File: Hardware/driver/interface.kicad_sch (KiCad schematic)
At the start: 34 parts

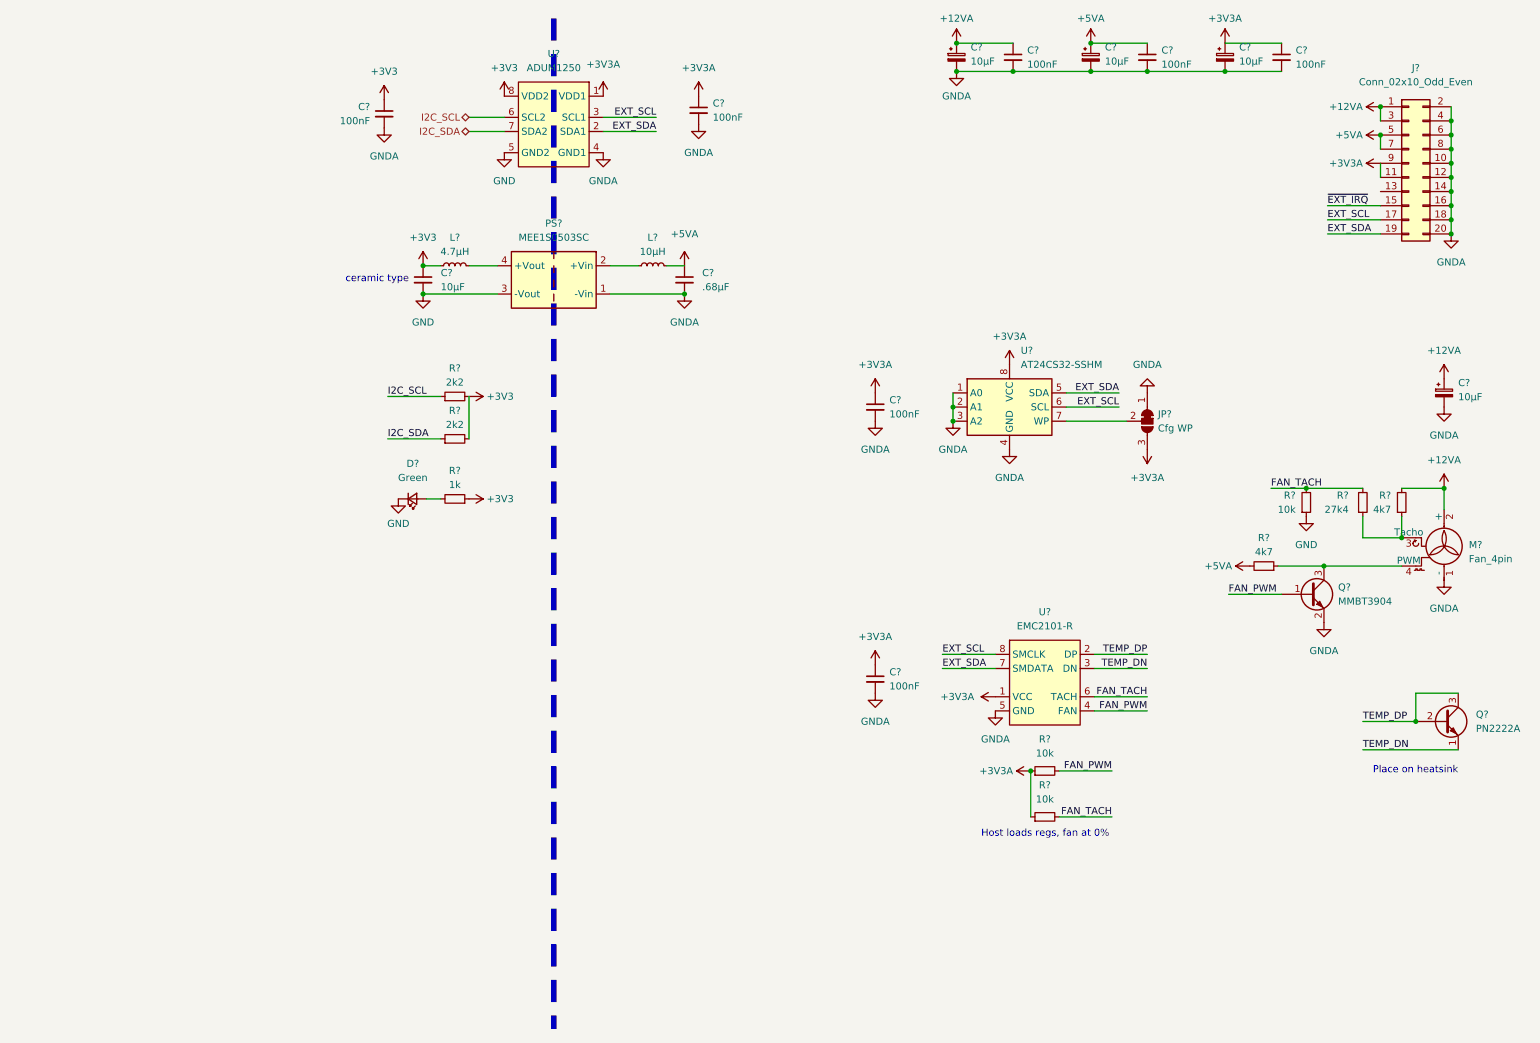
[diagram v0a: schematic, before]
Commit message: Placed all peripherals, start input
- Created footprints/symbols for some required I2C devices, including
  all DACs and ADCs, and placed them on the input section schematic

- Started work on heatsink footprint (C40-058-AE)

- Placed input connector for input. This is a pluggable screw terminal,
  which would then in turn connect to front panel jacks/banana plugs for
  external connectivity. This is good for roughly 20A, which is what the
  fuse (and our maximum rating for now) shall be
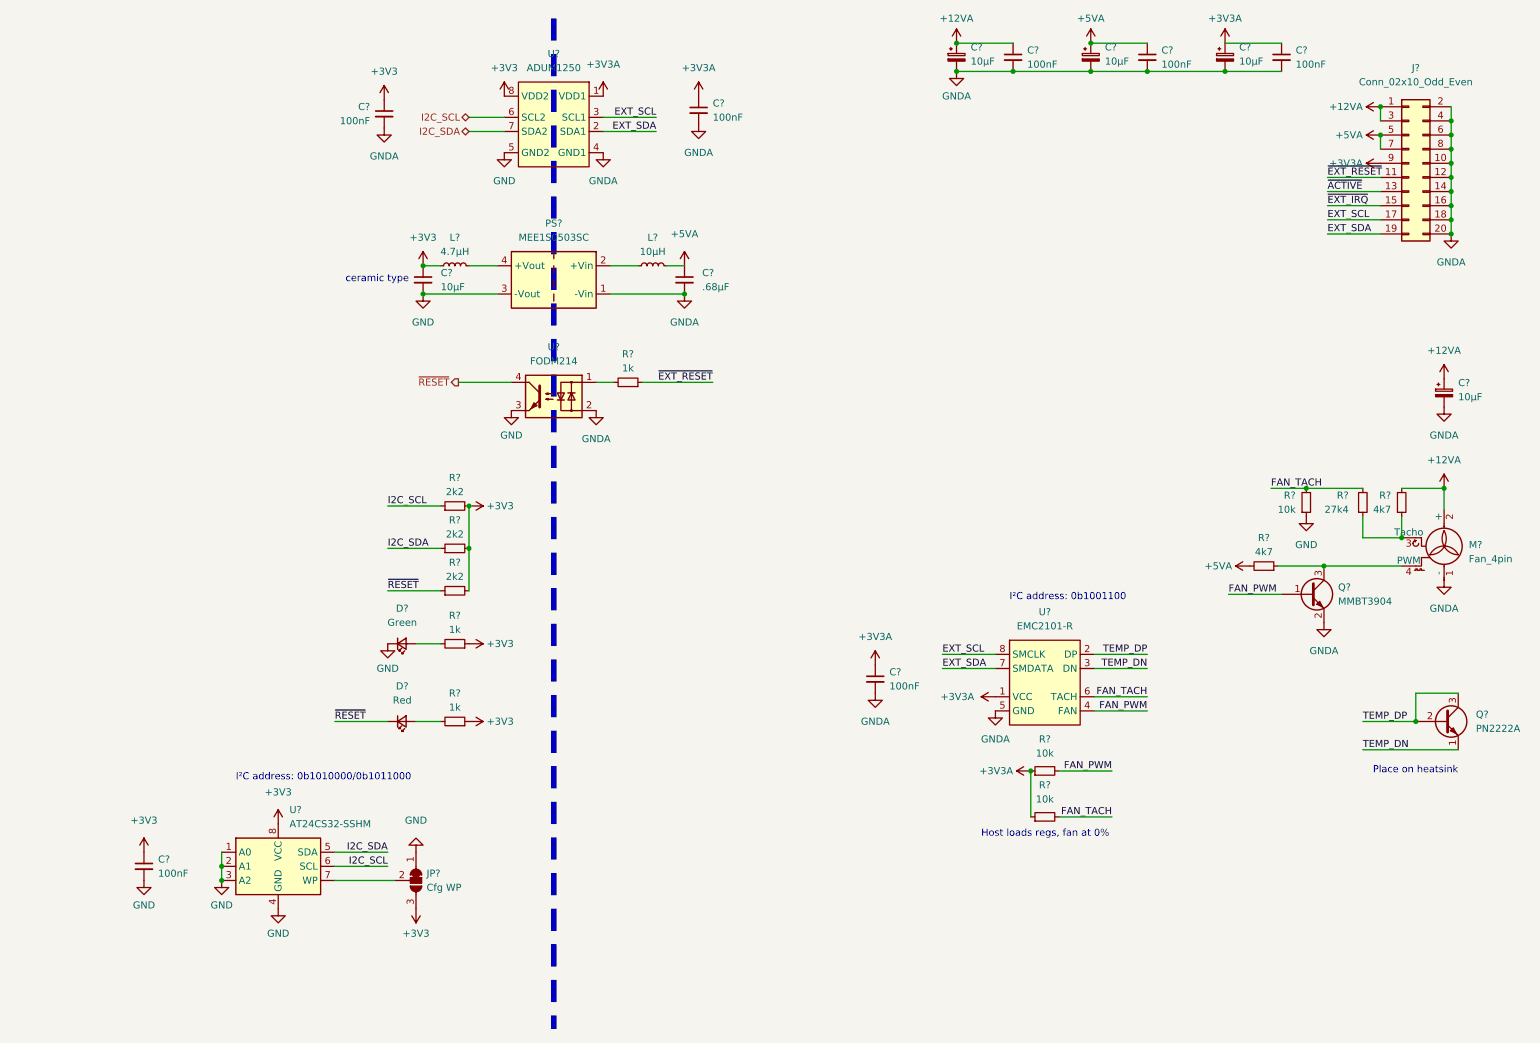
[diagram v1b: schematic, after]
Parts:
- added D?: Red, symbol Device:LED_Small
- added R?: 2k2, Resistor_SMD:R_0805_2012Metric_Pad1.20x1.40mm_HandSolder, symbol Device:R_Small
- added R? (x2): 1k, Resistor_SMD:R_0805_2012Metric_Pad1.20x1.40mm_HandSolder, symbol Device:R_Small
- added U?: FODM214, Package_SO:SOP-4_4.4x2.6mm_P1.27mm, symbol Isolator:FODM214
- C? (x7): footprint (none) -> Capacitor_SMD:C_0805_2012Metric_Pad1.18x1.45mm_HandSolder
- C?: footprint (none) -> Capacitor_SMD:C_0805_2012Metric_Pad1.18x1.45mm_HandSolder; MPN (none) -> CL21A106KPFNNNF
- C?: footprint (none) -> Capacitor_SMD:C_0805_2012Metric_Pad1.18x1.45mm_HandSolder; MPN (none) -> CL21B684JOFNNNE
- D?: MPN (none) -> 150080VS75000
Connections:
- net +3V3: now also C?.1, JP?.3 (B), U?.8 (VCC), R?.1, R?.2
- net +3V3A: no longer C?.1, J?.11 (Pin_11), JP?.3 (B), U?.8 (VCC)
- net EXT_SCL: no longer U?.6 (SCL)
- net EXT_SDA: no longer U?.5 (SDA)
- net GND: now also C?.2, JP?.1 (A), U?.1 (A0), U?.2 (A1), U?.3 (A2), U?.4 (GND), U?.3
- net GNDA: now also U?.2; no longer C?.2, JP?.1 (A), U?.1 (A0), U?.2 (A1), U?.3 (A2), U?.4 (GND)
- net I2C_SCL: now also U?.6 (SCL)
- net I2C_SDA: now also U?.5 (SDA)
- net ~{ACTIVE}: now reaches J?.13 (Pin_13)
- new net: R?.2, U?.1
- new net: D?.2 (A), R?.2
- new net ~{EXT_RESET}: J?.11 (Pin_11), R?.1
- new net ~{RESET}: D?.1 (K), R?.1, U?.4
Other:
- note added: "I²C address: 0b1001100"
- note added: "I²C address: 0b1010000/0b1011000"
- moved on the sheet: C?, D?, JP?, R?, U?

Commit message: Basic board layout shape
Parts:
- gave numbers to parts that had none: 39

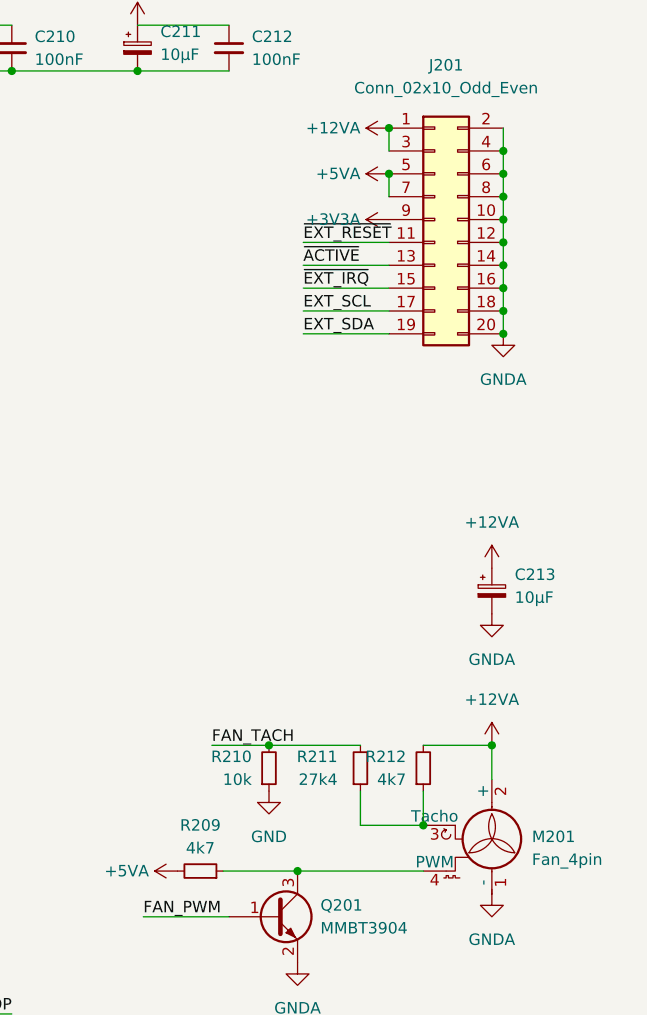
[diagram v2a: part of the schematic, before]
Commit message: Added mains supply input
- The driver board contains a switching mains supply that will give us
  the 12V the system needs, as if by magic

- More work on layout, basically placed the output MOSFETs and stuff
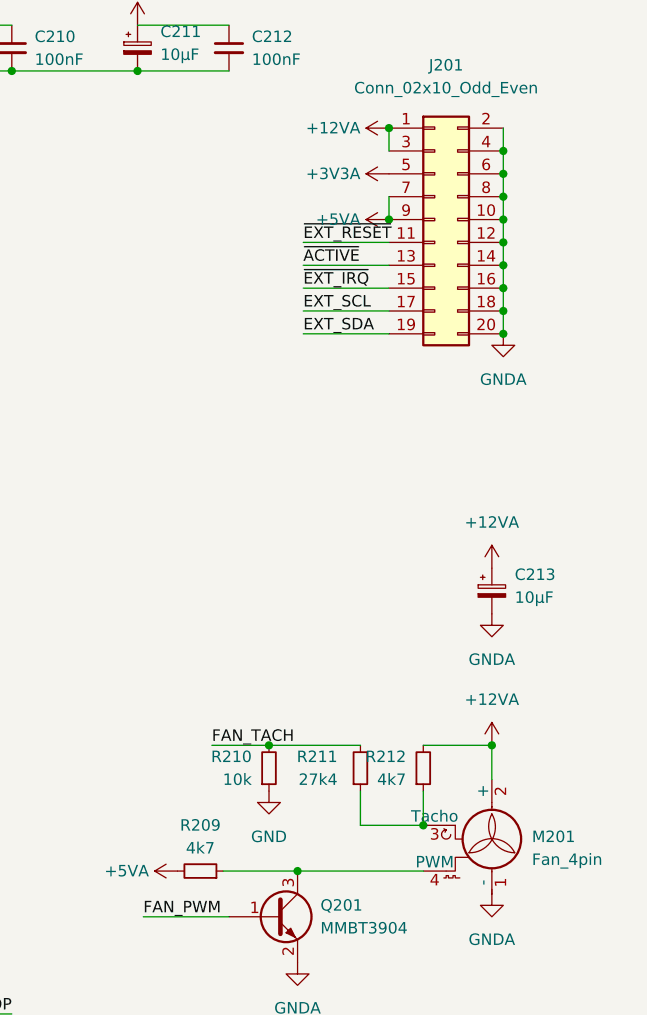
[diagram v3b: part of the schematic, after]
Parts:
- D201, D202: footprint (none) -> LED_SMD:LED_0805_2012Metric_Pad1.15x1.40mm_HandSolder
- J201: footprint Connector_PinHeader_1.27mm:PinHeader_2x10_P1.27mm_Vertical_SMD -> Connector_IDC:IDC-Header_2x10_P2.54mm_Vertical; MPN 20021521-00020T1LF, 20021121-00020C4LF -> T821120A1S100CEU
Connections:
- net +3V3A: now also J201.5 (Pin_5); no longer J201.9 (Pin_9)
- net +5VA: now also J201.9 (Pin_9); no longer J201.5 (Pin_5)
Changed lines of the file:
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@@
   (junction (at 194.31 149.86) (diameter 0) (color 0 0 0 0)
   )
-  (junction (at 257.175 35.56) (diameter 0) (color 0 0 0 0)
-  )
   (junction (at 93.345 102.235) (diameter 0) (color 0 0 0 0)
   )
@@
   )
   (junction (at 85.09 64.135) (diameter 0) (color 0 0 0 0)
+  )
+  (junction (at 257.175 40.64) (diameter 0) (color 0 0 0 0)
   )
   (wire (pts (xy 69.215 169.545) (xy 80.01 169.545))
@@
     (stroke (width 0) (type default) (color 0 0 0 0))
   )
+  (wire (pts (xy 257.175 38.1) (xy 257.175 40.64))
+    (stroke (width 0) (type default) (color 0 0 0 0))
+  )
   (wire (pts (xy 205.74 139.065) (xy 215.265 139.065))
     (stroke (width 0) (type default) (color 0 0 0 0))
@@
   )
   (wire (pts (xy 247.65 45.72) (xy 257.175 45.72))
-    (stroke (width 0) (type default) (color 0 0 0 0))
-  )
-  (wire (pts (xy 257.175 35.56) (xy 257.175 38.1))
     (stroke (width 0) (type default) (color 0 0 0 0))
   )
@@
     (pin "1")
   )
-  (symbol (lib_id "power:+5VA") (at 257.175 35.56 90) (unit 1)
-    (in_bom yes) (on_board yes) (fields_autoplaced)
-    (property "Reference" "#PWR0239" (id 0) (at 260.985 35.56 0)
-      (effects (font (size 1.27 1.27)) hide)
-    )
-    (property "Value" "+5VA" (id 1) (at 254 35.5599 90)
-      (effects (font (size 1.27 1.27)) (justify left))
-    )
-    (property "Footprint" "" (id 2) (at 257.175 35.56 0)
-      (effects (font (size 1.27 1.27)) hide)
-    )
-    (property "Datasheet" "" (id 3) (at 257.175 35.56 0)
+  (symbol (lib_id "power:+5VA") (at 257.175 40.64 90) (unit 1)
+    (in_bom yes) (on_board yes) (fields_autoplaced)
+    (property "Reference" "#PWR0239" (id 0) (at 260.985 40.64 0)
+      (effects (font (size 1.27 1.27)) hide)
+    )
+    (property "Value" "+5VA" (id 1) (at 254 40.6399 90)
+      (effects (font (size 1.27 1.27)) (justify left))
+    )
+    (property "Footprint" "" (id 2) (at 257.175 40.64 0)
+      (effects (font (size 1.27 1.27)) hide)
+    )
+    (property "Datasheet" "" (id 3) (at 257.175 40.64 0)
       (effects (font (size 1.27 1.27)) hide)
     )
@@
     (pin "2")
   )
-  (symbol (lib_id "programmable-load:+3V3A") (at 257.175 40.64 90) (unit 1)
-    (in_bom yes) (on_board yes) (fields_autoplaced)
-    (property "Reference" "#PWR0240" (id 0) (at 260.985 40.64 0)
-      (effects (font (size 1.27 1.27)) hide)
-    )
-    (property "Value" "+3V3A" (id 1) (at 254 40.6399 90)
-      (effects (font (size 1.27 1.27)) (justify left))
-    )
-    (property "Footprint" "" (id 2) (at 257.175 40.64 0)
-      (effects (font (size 1.27 1.27)) hide)
-    )
-    (property "Datasheet" "" (id 3) (at 257.175 40.64 0)
+  (symbol (lib_id "programmable-load:+3V3A") (at 257.175 35.56 90) (unit 1)
+    (in_bom yes) (on_board yes) (fields_autoplaced)
+    (property "Reference" "#PWR0240" (id 0) (at 260.985 35.56 0)
+      (effects (font (size 1.27 1.27)) hide)
+    )
+    (property "Value" "+3V3A" (id 1) (at 254 35.5599 90)
+      (effects (font (size 1.27 1.27)) (justify left))
+    )
+    (property "Footprint" "" (id 2) (at 257.175 35.56 0)
+      (effects (font (size 1.27 1.27)) hide)
+    )
+    (property "Datasheet" "" (id 3) (at 257.175 35.56 0)
       (effects (font (size 1.27 1.27)) hide)
     )
@@
     (property "Reference" "D202" (id 0) (at 81.3435 134.62 0))
     (property "Value" "Red" (id 1) (at 81.3435 137.16 0))
-    (property "Footprint" "" (id 2) (at 81.28 140.97 90)
+    (property "Footprint" "LED_SMD:LED_0805_2012Metric_Pad1.15x1.40mm_HandSolder" (id 2) (at 81.28 140.97 90)
       (effects (font (size 1.27 1.27)) hide)
     )
@@
     (property "Reference" "D201" (id 0) (at 81.3435 120.65 0))
     (property "Value" "Green" (id 1) (at 81.3435 123.19 0))
-    (property "Footprint" "" (id 2) (at 81.28 127 90)
+    (property "Footprint" "LED_SMD:LED_0805_2012Metric_Pad1.15x1.40mm_HandSolder" (id 2) (at 81.28 127 90)
       (effects (font (size 1.27 1.27)) hide)
     )
@@
     (property "Reference" "J201" (id 0) (at 263.525 23.495 0))
     (property "Value" "Conn_02x10_Odd_Even" (id 1) (at 263.525 26.035 0))
-    (property "Footprint" "Connector_PinHeader_1.27mm:PinHeader_2x10_P1.27mm_Vertical_SMD" (id 2) (at 262.255 40.64 0)
+    (property "Footprint" "Connector_IDC:IDC-Header_2x10_P2.54mm_Vertical" (id 2) (at 262.255 40.64 0)
       (effects (font (size 1.27 1.27)) hide)
     )
@@
       (effects (font (size 1.27 1.27)) hide)
     )
-    (property "MPN" "20021521-00020T1LF, 20021121-00020C4LF" (id 4) (at 262.255 40.64 0)
-      (effects (font (size 1.27 1.27)) hide)
-    )
+    (property "MPN" "T821120A1S100CEU" (id 4) (at 262.255 40.64 0)
+      (effects (font (size 1.27 1.27)) hide)
+    )
